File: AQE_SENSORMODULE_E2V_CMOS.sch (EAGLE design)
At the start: 35 parts, among them J1 440055-4, J2 AVR_SPI_PRG_6NS, U1 V_REG_LDOSMD, U2 V_REG_LDOSMD, U3 MCP41XXX

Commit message: incorporated several changes based on review comments
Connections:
- net /POT_CS: now also MCU.PD2(INT0/PCINT18)
- net AGND: now also R3.1, R5.1
- net GND: no longer R3.1, R5.1
- net HEATER_EN: now also MCU.PD0(PCINT16); no longer MCU.PC3(ADC3/PCINT11)
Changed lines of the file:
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@@
 <setting verticaltext="up"/>
 </settings>
-<grid distance="0.05" unitdist="inch" unit="inch" style="lines" multiple="1" display="no" altdistance="0.01" altunitdist="inch" altunit="inch"/>
+<grid distance="0.1" unitdist="inch" unit="inch" style="lines" multiple="1" display="no" altdistance="0.01" altunitdist="inch" altunit="inch"/>
 <layers>
 <layer number="1" name="Top" color="4" fill="1" visible="no" active="no"/>
@@
 <part name="U$3" library="wicked-device" deviceset="PLANE_COUPLER" device=""/>
 <part name="SUPPLY4" library="supply2" deviceset="GND" device=""/>
-<part name="SUPPLY5" library="supply2" deviceset="GND" device=""/>
 </parts>
 <sheets>
@@
 <instance part="U$3" gate="G$1" x="342.9" y="46.99"/>
 <instance part="SUPPLY4" gate="GND" x="327.66" y="41.91"/>
-<instance part="SUPPLY5" gate="GND" x="95.25" y="17.78"/>
 </instances>
 <busses>
@@
 <wire x1="327.66" y1="46.99" x2="327.66" y2="44.45" width="0.1524" layer="91"/>
 </segment>
-<segment>
-<pinref part="R3" gate="G$1" pin="1"/>
-<wire x1="104.14" y1="29.21" x2="104.14" y2="20.32" width="0.1524" layer="91"/>
-<pinref part="R5" gate="G$1" pin="1"/>
-<wire x1="86.36" y1="35.56" x2="86.36" y2="20.32" width="0.1524" layer="91"/>
-<wire x1="86.36" y1="20.32" x2="95.25" y2="20.32" width="0.1524" layer="91"/>
-<pinref part="SUPPLY5" gate="GND" pin="GND"/>
-<wire x1="95.25" y1="20.32" x2="104.14" y2="20.32" width="0.1524" layer="91"/>
-<junction x="95.25" y="20.32"/>
-</segment>
 </net>
 <net name="/RESET" class="0">
@@
 <label x="387.35" y="207.01" size="1.778" layer="95" rot="R180" xref="yes"/>
 </segment>
+<segment>
+<pinref part="MCU" gate="G$1" pin="PD2(INT0/PCINT18)"/>
+<wire x1="271.78" y1="180.34" x2="292.1" y2="180.34" width="0.1524" layer="91"/>
+<label x="292.1" y="180.34" size="1.778" layer="95" xref="yes"/>
+</segment>
 </net>
 <net name="AGND" class="0">
@@
 <label x="179.07" y="218.44" size="1.778" layer="95" rot="R180" xref="yes"/>
 </segment>
+<segment>
+<pinref part="R3" gate="G$1" pin="1"/>
+<wire x1="104.14" y1="29.21" x2="104.14" y2="20.32" width="0.1524" layer="91"/>
+<pinref part="R5" gate="G$1" pin="1"/>
+<wire x1="86.36" y1="35.56" x2="86.36" y2="20.32" width="0.1524" layer="91"/>
+<wire x1="86.36" y1="20.32" x2="104.14" y2="20.32" width="0.1524" layer="91"/>
+<wire x1="86.36" y1="20.32" x2="78.74" y2="20.32" width="0.1524" layer="91"/>
+<junction x="86.36" y="20.32"/>
+<label x="78.74" y="20.32" size="1.778" layer="95" rot="R180"/>
+</segment>
 </net>
 <net name="HEATER_EN" class="0">
@@
 </segment>
 <segment>
-<pinref part="MCU" gate="G$1" pin="PC3(ADC3/PCINT11)"/>
-<wire x1="271.78" y1="198.12" x2="308.61" y2="198.12" width="0.1524" layer="91"/>
-<label x="308.61" y="198.12" size="1.778" layer="95" xref="yes"/>
-</segment>
-</net>
+<wire x1="271.78" y1="185.42" x2="308.61" y2="185.42" width="0.1524" layer="91"/>
+<label x="308.61" y="185.42" size="1.778" layer="95" xref="yes"/>
+<pinref part="MCU" gate="G$1" pin="PD0(PCINT16)"/>
+</segment>
+</net>

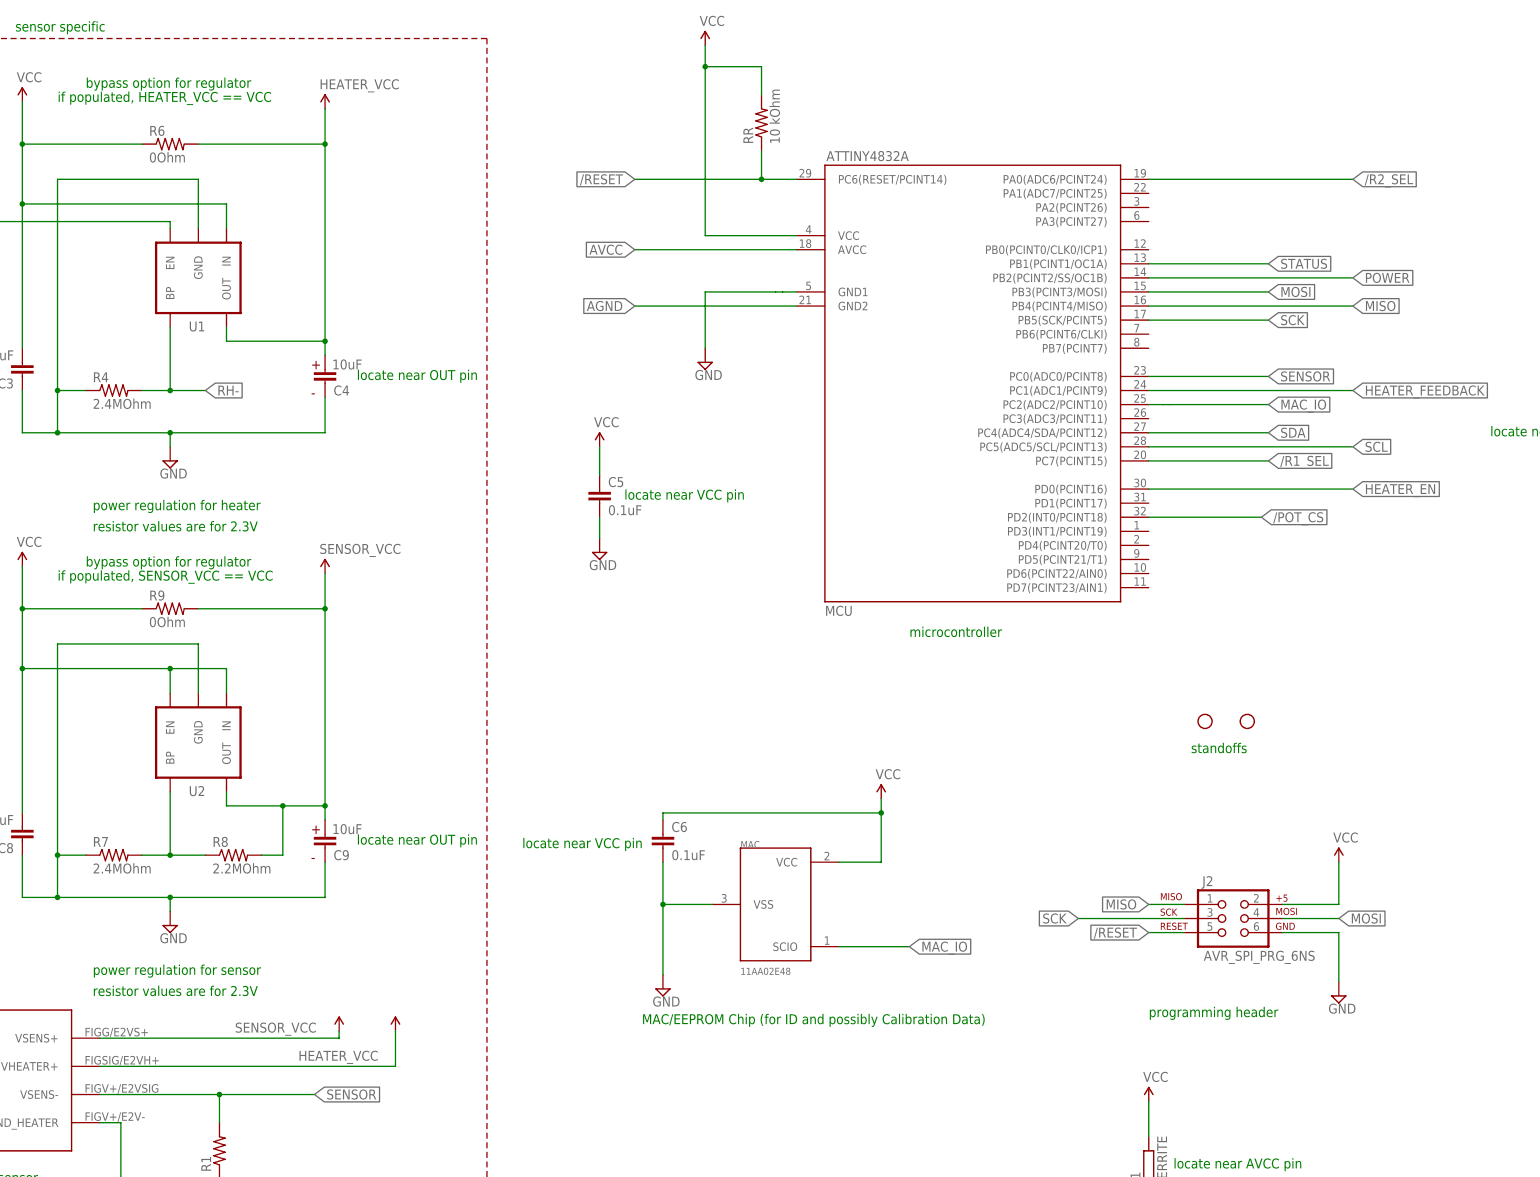
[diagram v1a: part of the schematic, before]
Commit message: updated schematic and board to make attiny48 pinout compatible with egg shield
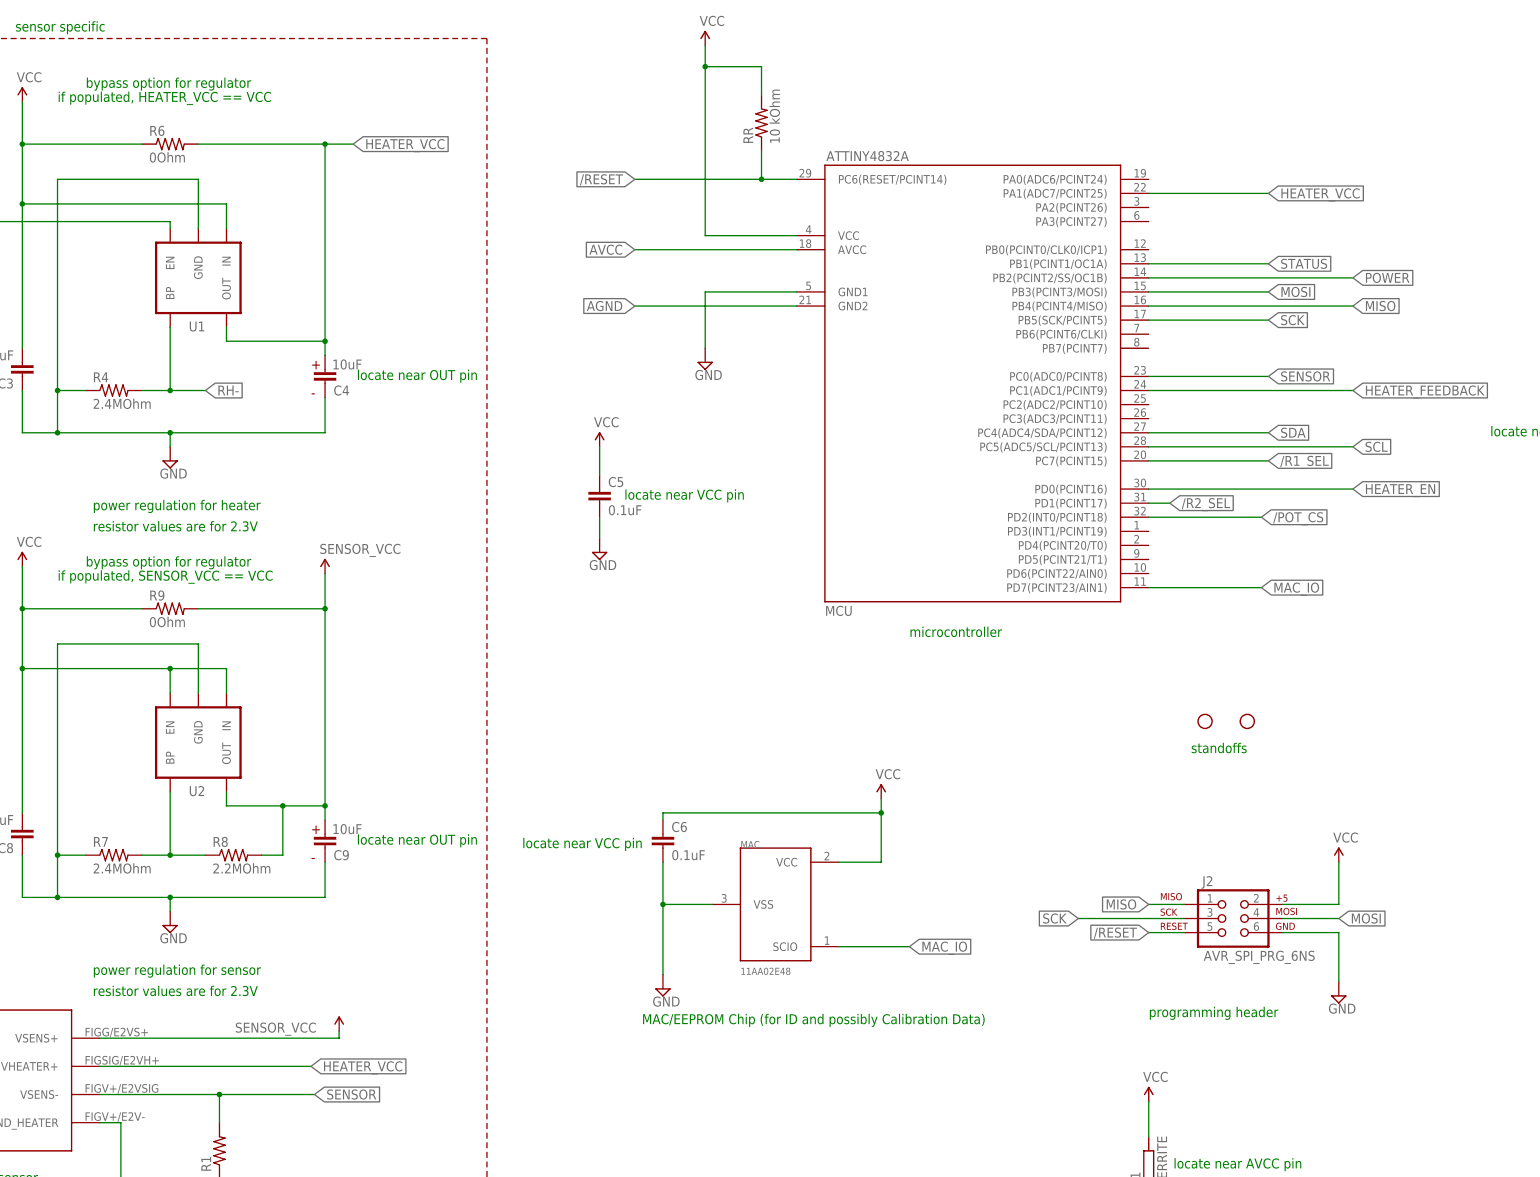
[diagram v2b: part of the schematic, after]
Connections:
- net /R2_SEL: now also MCU.PD1(PCINT17); no longer MCU.PA0(ADC6/PCINT24)
- net HEATER_VCC: now also MCU.PA1(ADC7/PCINT25)
- net MAC_IO: now also MCU.PD7(PCINT23/AIN1); no longer MCU.PC2(ADC2/PCINT10)
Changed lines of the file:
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@@
 <setting verticaltext="up"/>
 </settings>
-<grid distance="0.1" unitdist="inch" unit="inch" style="lines" multiple="1" display="no" altdistance="0.01" altunitdist="inch" altunit="inch"/>
+<grid distance="0.05" unitdist="inch" unit="inch" style="lines" multiple="1" display="no" altdistance="0.01" altunitdist="inch" altunit="inch"/>
 <layers>
 <layer number="1" name="Top" color="4" fill="1" visible="no" active="no"/>
@@
 <part name="SUPPLY3" library="supply2" deviceset="GND" device=""/>
 <part name="P+3" library="SparkFun" deviceset="VCC" device=""/>
-<part name="HEATER_VCC" library="SparkFun" deviceset="1.8V" device="" value="HEATER_VCC"/>
 <part name="C3" library="SparkFun" deviceset="CAP" device="0603-CAP" value="0.1uF"/>
 <part name="C4" library="wicked-device" deviceset="EEE-1EA100WR" device="" value="10uF"/>
@@
 <part name="R4" library="SparkFun" deviceset="RESISTOR" device="0805-RES" value="2.4MOhm"/>
 <part name="U1" library="SparkFun" deviceset="V_REG_LDO" device="SMD"/>
-<part name="U$1" library="SparkFun" deviceset="1.8V" device="" value="HEATER_VCC"/>
 <part name="R2" library="SparkFun" deviceset="RESISTOR" device="0805-RES"/>
 <part name="R3" library="SparkFun" deviceset="RESISTOR" device="0805-RES"/>
@@
 <instance part="SUPPLY3" gate="GND" x="95.25" y="190.5"/>
 <instance part="P+3" gate="1" x="68.58" y="255.27"/>
-<instance part="HEATER_VCC" gate="G$1" x="123.19" y="254" smashed="yes">
-<attribute name="VALUE" x="122.174" y="257.556" size="1.778" layer="96"/>
-</instance>
 <instance part="C3" gate="G$1" x="68.58" y="208.28" rot="R180"/>
 <instance part="C4" gate="G$1" x="123.19" y="204.47" smashed="yes">
@@
 <instance part="U1" gate="G$1" x="100.33" y="222.25" smashed="yes" rot="R270">
 <attribute name="NAME" x="101.6" y="215.646" size="1.778" layer="95" rot="R180"/>
-</instance>
-<instance part="U$1" gate="G$1" x="135.89" y="87.63" smashed="yes">
-<attribute name="VALUE" x="118.364" y="82.296" size="1.778" layer="96"/>
 </instance>
 <instance part="R2" gate="G$1" x="104.14" y="49.53" rot="R90"/>
@@
 <segment>
 <pinref part="MCU" gate="G$1" pin="GND1"/>
-<wire x1="208.28" y1="220.98" x2="205.74" y2="220.98" width="0.1524" layer="91"/>
 <pinref part="SUPPLY1" gate="GND" pin="GND"/>
-<wire x1="205.74" y1="220.98" x2="204.47" y2="220.98" width="0.1524" layer="91"/>
-<wire x1="204.47" y1="220.98" x2="191.77" y2="220.98" width="0.1524" layer="91"/>
+<wire x1="208.28" y1="220.98" x2="191.77" y2="220.98" width="0.1524" layer="91"/>
 <wire x1="191.77" y1="220.98" x2="191.77" y2="210.82" width="0.1524" layer="91"/>
 </segment>
@@
 </segment>
 <segment>
-<label x="308.61" y="241.3" size="1.778" layer="95" xref="yes"/>
-<pinref part="MCU" gate="G$1" pin="PA0(ADC6/PCINT24)"/>
-<wire x1="308.61" y1="241.3" x2="271.78" y2="241.3" width="0.1524" layer="91"/>
+<label x="275.59" y="182.88" size="1.778" layer="95" xref="yes"/>
+<wire x1="275.59" y1="182.88" x2="271.78" y2="182.88" width="0.1524" layer="91"/>
+<pinref part="MCU" gate="G$1" pin="PD1(PCINT17)"/>
 </segment>
 </net>
 <net name="MAC_IO" class="0">
 <segment>
-<wire x1="275.59" y1="200.66" x2="293.37" y2="200.66" width="0.1524" layer="91"/>
-<label x="293.37" y="200.66" size="1.778" layer="95" xref="yes"/>
-<pinref part="MCU" gate="G$1" pin="PC2(ADC2/PCINT10)"/>
-<wire x1="271.78" y1="200.66" x2="274.32" y2="200.66" width="0.1524" layer="91"/>
-<wire x1="274.32" y1="200.66" x2="275.59" y2="200.66" width="0.1524" layer="91"/>
+<wire x1="271.78" y1="167.64" x2="292.1" y2="167.64" width="0.1524" layer="91"/>
+<label x="292.1" y="167.64" size="1.778" layer="95" xref="yes"/>
+<pinref part="MCU" gate="G$1" pin="PD7(PCINT23/AIN1)"/>
 </segment>
 <segment>
@@
 <net name="HEATER_VCC" class="0">
 <segment>
-<pinref part="HEATER_VCC" gate="G$1" pin="1.8V"/>
-<wire x1="123.19" y1="254" x2="123.19" y2="247.65" width="0.1524" layer="91"/>
+<wire x1="128.27" y1="247.65" x2="123.19" y2="247.65" width="0.1524" layer="91"/>
 <pinref part="C4" gate="G$1" pin="1"/>
 <wire x1="123.19" y1="247.65" x2="123.19" y2="212.09" width="0.1524" layer="91"/>
@@
 <wire x1="105.41" y1="214.63" x2="105.41" y2="212.09" width="0.1524" layer="91"/>
 <wire x1="105.41" y1="212.09" x2="123.19" y2="212.09" width="0.1524" layer="91"/>
+<label x="128.27" y="247.65" size="1.778" layer="95" xref="yes"/>
 </segment>
 <segment>
 <pinref part="U$4" gate="G$1" pin="VHEATER+"/>
-<wire x1="82.55" y1="81.28" x2="135.89" y2="81.28" width="0.1524" layer="91"/>
-<wire x1="135.89" y1="81.28" x2="135.89" y2="87.63" width="0.1524" layer="91"/>
-<pinref part="U$1" gate="G$1" pin="1.8V"/>
+<wire x1="82.55" y1="81.28" x2="120.65" y2="81.28" width="0.1524" layer="91"/>
+<label x="120.65" y="81.28" size="1.778" layer="95" xref="yes"/>
 </segment>
 <segment>
@@
 <label x="387.35" y="196.85" size="1.778" layer="95" rot="R180" xref="yes"/>
 </segment>
-</net>
+<segment>
+<pinref part="MCU" gate="G$1" pin="PA1(ADC7/PCINT25)"/>
+<wire x1="271.78" y1="238.76" x2="293.37" y2="238.76" width="0.1524" layer="91"/>
+<label x="293.37" y="238.76" size="1.778" layer="95" xref="yes"/>
+</segment>
+</net>
